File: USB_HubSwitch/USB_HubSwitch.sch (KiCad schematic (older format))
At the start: 22 parts, among them J1 690-005-299-043, J2 690-005-299-043, J3 690-005-299-043, J4 M20-9990246, J5 UE27AC54100, U1 MAX40200AUK, U2 MAX40200AUK, U3 MAX40200AUK, U4 TS3USB30EDGSR

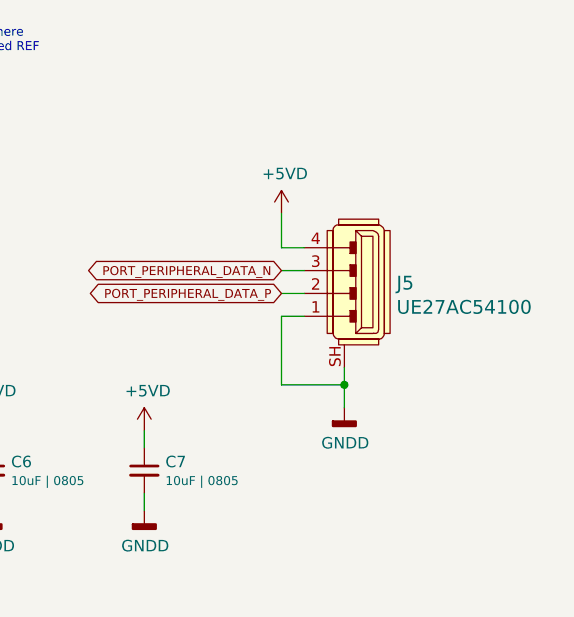
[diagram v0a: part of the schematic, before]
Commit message: Fixed USB Receptacle Pinout
this shall be used... fixed TYPE A pinout, was flipped vertically
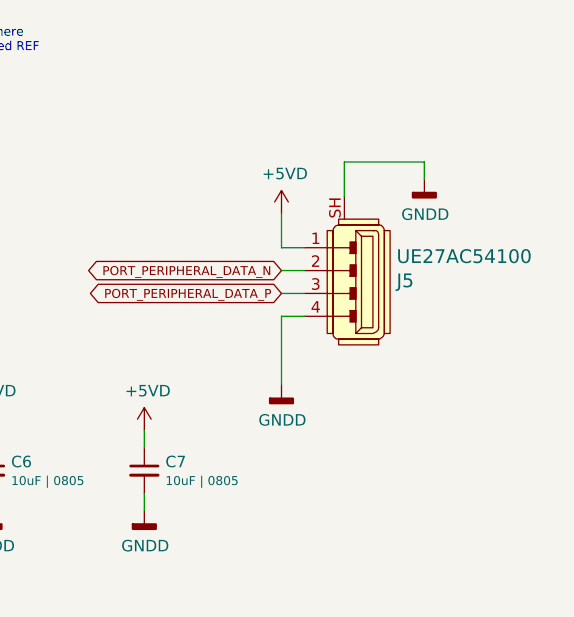
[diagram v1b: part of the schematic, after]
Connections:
- net +5VD: now also J5.1; no longer J5.4
- net GNDD: now also J5.4; no longer J5.1
- net PORT_PERIPHERAL_DATA_N: now also J5.2; no longer J5.3
- net PORT_PERIPHERAL_DATA_P: now also J5.3; no longer J5.2
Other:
- moved on the sheet: J5
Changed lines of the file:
@@
 EESchema Schematic File Version 4
+LIBS:USB_HubSwitch-cache
 EELAYER 30 0
 EELAYER END
@@
 L dk_USB-DVI-HDMI-Connectors:UE27AC54100 J5
 U 1 1 5DB3B81C
-P 13200 5800
-F 0 "J5" H 13097 5845 60  0000 R CNN
-F 1 "UE27AC54100" H 13097 5739 60  0000 R CNN
-F 2 "digikey-footprints:USB_A_Female_UE27AC54100" H 13400 6000 60  0001 L CNN
-F 3 "https://www.amphenolcanada.com/ProductSearch/drawings/AC/UE27ACX4X0X.pdf" H 13400 6100 60  0001 L CNN
-F 4 "UE27AC54100-ND" H 13400 6200 60  0001 L CNN "Digi-Key_PN"
-F 5 "UE27AC54100" H 13400 6300 60  0001 L CNN "MPN"
-F 6 "Connectors, Interconnects" H 13400 6400 60  0001 L CNN "Category"
-F 7 "USB, DVI, HDMI Connectors" H 13400 6500 60  0001 L CNN "Family"
-F 8 "https://www.amphenolcanada.com/ProductSearch/drawings/AC/UE27ACX4X0X.pdf" H 13400 6600 60  0001 L CNN "DK_Datasheet_Link"
-F 9 "/product-detail/en/amphenol-icc-commercial-products/UE27AC54100/UE27AC54100-ND/1972253" H 13400 6700 60  0001 L CNN "DK_Detail_Page"
-F 10 "CONN RCPT USB2.0 TYPEA 4POS R/A" H 13400 6800 60  0001 L CNN "Description"
-F 11 "Amphenol ICC (Commercial Products)" H 13400 6900 60  0001 L CNN "Manufacturer"
-F 12 "Active" H 13400 7000 60  0001 L CNN "Status"
-	1    13200 5800
-	-1   0    0    -1
-$EndComp
-Wire Wire Line
-	13075 6125 13075 6200
-Wire Wire Line
-	13075 6200 12800 6200
+P 13200 5700
+F 0 "J5" H 13097 5745 60  0000 R CNN
+F 1 "UE27AC54100" H 13097 5639 60  0000 R CNN
+F 2 "digikey-footprints:USB_A_Female_UE27AC54100" H 13400 5900 60  0001 L CNN
+F 3 "https://www.amphenolcanada.com/ProductSearch/drawings/AC/UE27ACX4X0X.pdf" H 13400 6000 60  0001 L CNN
+F 4 "UE27AC54100-ND" H 13400 6100 60  0001 L CNN "Digi-Key_PN"
+F 5 "UE27AC54100" H 13400 6200 60  0001 L CNN "MPN"
+F 6 "Connectors, Interconnects" H 13400 6300 60  0001 L CNN "Category"
+F 7 "USB, DVI, HDMI Connectors" H 13400 6400 60  0001 L CNN "Family"
+F 8 "https://www.amphenolcanada.com/ProductSearch/drawings/AC/UE27ACX4X0X.pdf" H 13400 6500 60  0001 L CNN "DK_Datasheet_Link"
+F 9 "/product-detail/en/amphenol-icc-commercial-products/UE27AC54100/UE27AC54100-ND/1972253" H 13400 6600 60  0001 L CNN "DK_Detail_Page"
+F 10 "CONN RCPT USB2.0 TYPEA 4POS R/A" H 13400 6700 60  0001 L CNN "Description"
+F 11 "Amphenol ICC (Commercial Products)" H 13400 6800 60  0001 L CNN "Manufacturer"
+F 12 "Active" H 13400 6900 60  0001 L CNN "Status"
+	1    13200 5700
+	-1   0    0    1
+$EndComp
 Wire Wire Line
 	12800 6200 12800 5900
 Wire Wire Line
 	12800 5900 12900 5900
-Wire Wire Line
-	13075 6200 13075 6300
-Connection ~ 13075 6200
 $Comp
 L power:GNDD #PWR0101
 U 1 1 5DB41BC7
-P 13075 6300
-F 0 "#PWR0101" H 13075 6050 50  0001 C CNN
-F 1 "GNDD" H 13079 6145 50  0000 C CNN
-F 2 "" H 13075 6300 50  0001 C CNN
-F 3 "" H 13075 6300 50  0001 C CNN
-	1    13075 6300
+P 12800 6200
+F 0 "#PWR0101" H 12800 5950 50  0001 C CNN
+F 1 "GNDD" H 12804 6045 50  0000 C CNN
+F 2 "" H 12800 6200 50  0001 C CNN
+F 3 "" H 12800 6200 50  0001 C CNN
+	1    12800 6200
 	1    0    0    -1
 $EndComp
@@
 Text Notes 7575 6300 0    59   ~ 12
 S = L, D=D1
+$Comp
+L power:GNDD #PWR?
+U 1 1 5DDBD562
+P 13425 5300
+F 0 "#PWR?" H 13425 5050 50  0001 C CNN
+F 1 "GNDD" H 13429 5145 50  0000 C CNN
+F 2 "" H 13425 5300 50  0001 C CNN
+F 3 "" H 13425 5300 50  0001 C CNN
+	1    13425 5300
+	1    0    0    -1
+$EndComp
+Wire Wire Line
+	13425 5300 13425 5225
+Wire Wire Line
+	13425 5225 13075 5225
+Wire Wire Line
+	13075 5225 13075 5375
 $EndSCHEMATC
